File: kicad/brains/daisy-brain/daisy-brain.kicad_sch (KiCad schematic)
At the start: 8 parts, among them J15 Conn_01x06, J16 Conn_01x06, J17 Conn_01x06, J18 Conn_01x06, J2 Conn_01x20, J4 Conn_02x20_Odd_Even, J5 Conn_02x20_Odd_Even

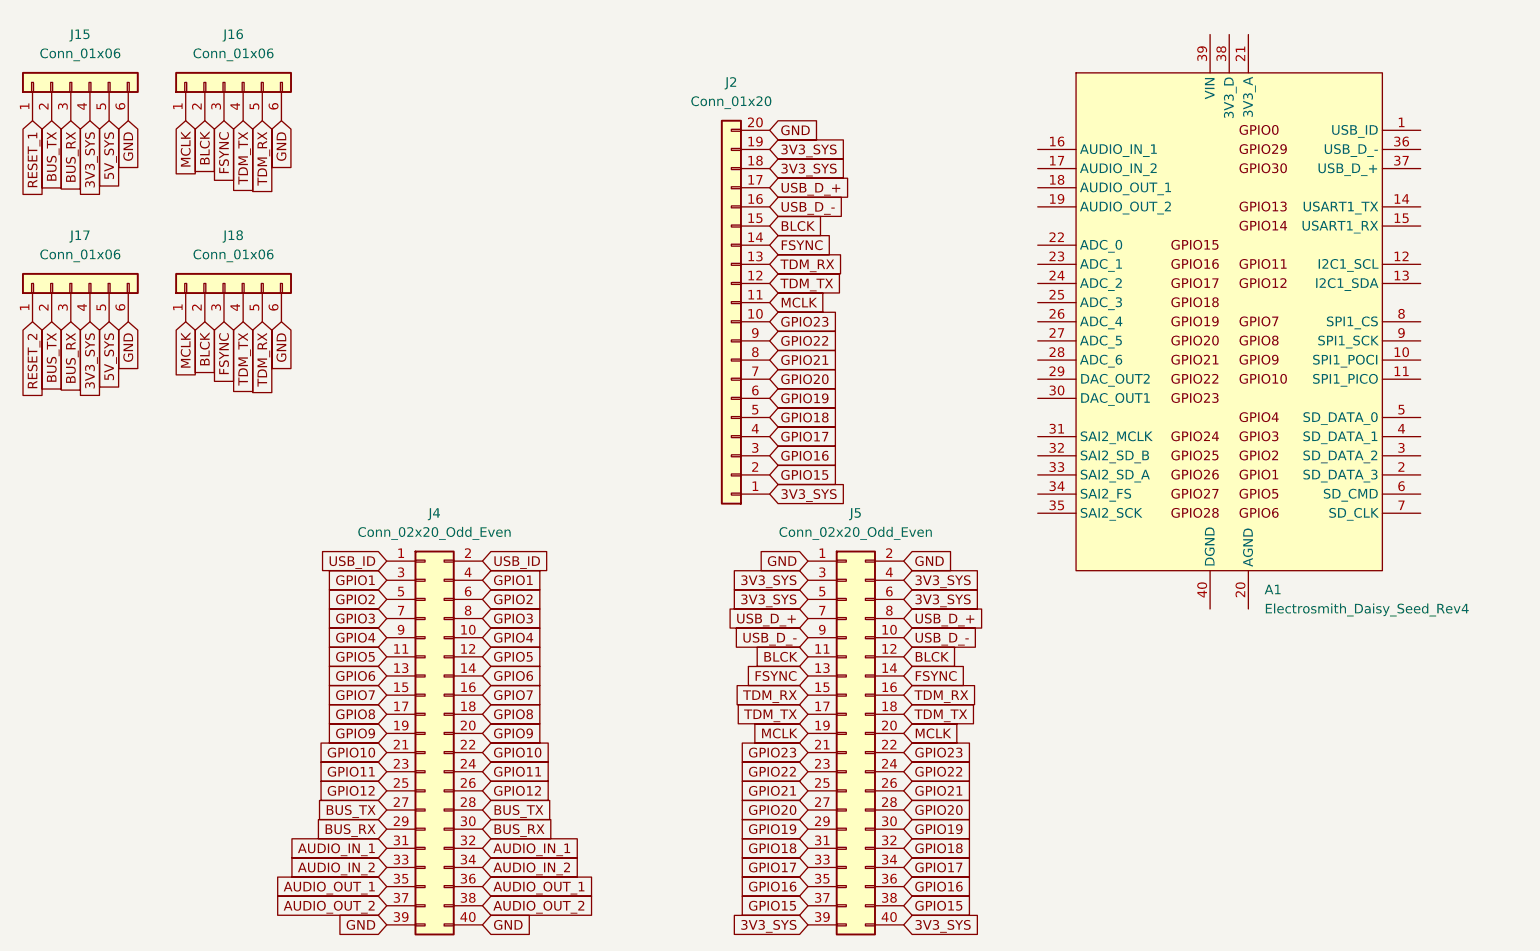
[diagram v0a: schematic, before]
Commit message: Update card template and MIDI Buddy
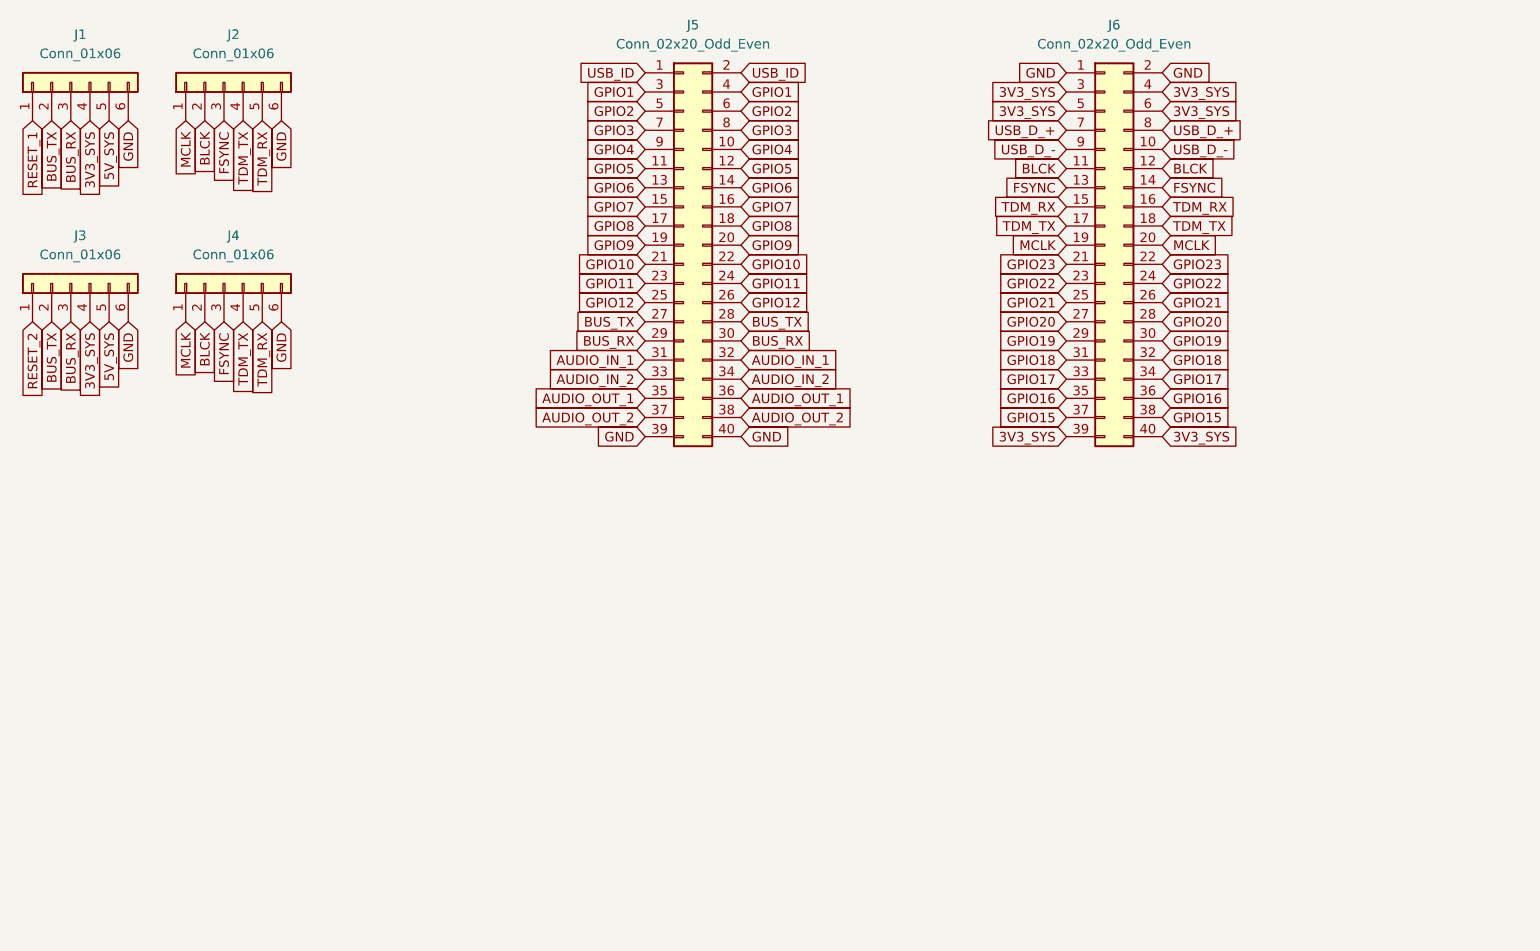
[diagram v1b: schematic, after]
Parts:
- removed A1: Electrosmith_Daisy_Seed_Rev4, Module:Electrosmith_Daisy_Seed, symbol MCU_Module:Electrosmith_Daisy_Seed_Rev4
- removed J2: Conn_01x20, Connector_PinSocket_2.54mm:PinSocket_1x20_P2.54mm_Vertical, symbol Connector_Generic:Conn_01x20
- renumbered J15 to J1, J16 to J2, J17 to J3, J18 to J4, J4 to J5, J5 to J6
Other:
- moved on the sheet: J5, J6
